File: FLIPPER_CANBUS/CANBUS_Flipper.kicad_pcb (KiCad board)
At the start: 2 copper layers, 67 x 21.3 mm, 33 parts, among them J1 Conn_01x08_Socket, J2 Conn_01x10_Socket, J3 Conn_01x02, J4 Conn_01x02_Socket, U1 MCP2515-xST, U2 MAX3051, Y1 16 Mhz

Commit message: feat(hw): label updated
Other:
- board text removed: "FLIPPER SHIELD CANBUS V1.0"
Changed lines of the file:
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@@
 		(layer "Edge.Cuts")
 	)
-	(gr_text "FLIPPER SHIELD\nCANBUS V1.0"
+	(gr_text "FLIPPER SHIELD\nCANBUS V1.1"
 		(at 139.446 100.584 0)
 		(layer "B.SilkS")

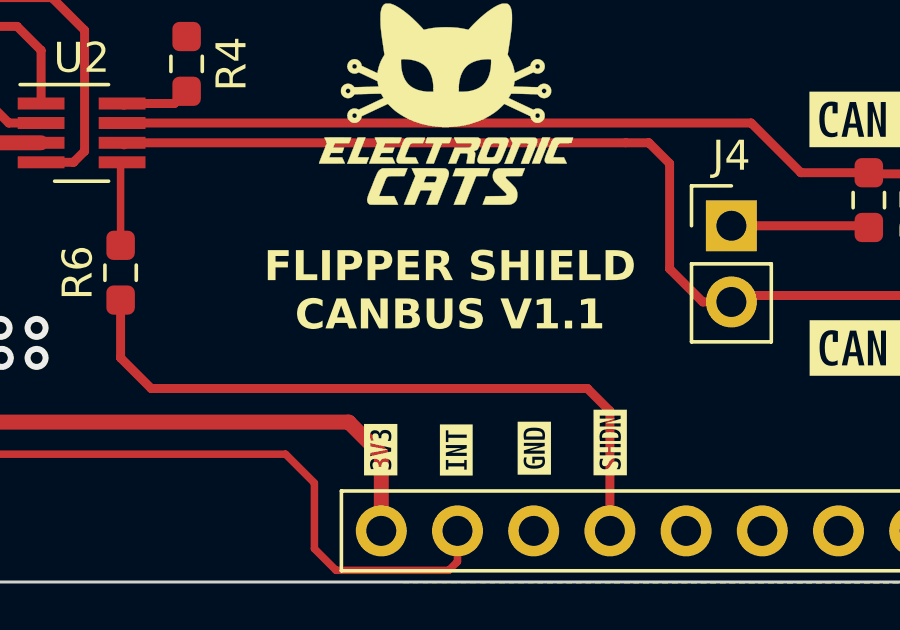
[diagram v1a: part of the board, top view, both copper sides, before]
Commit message: feat: version Label got updated
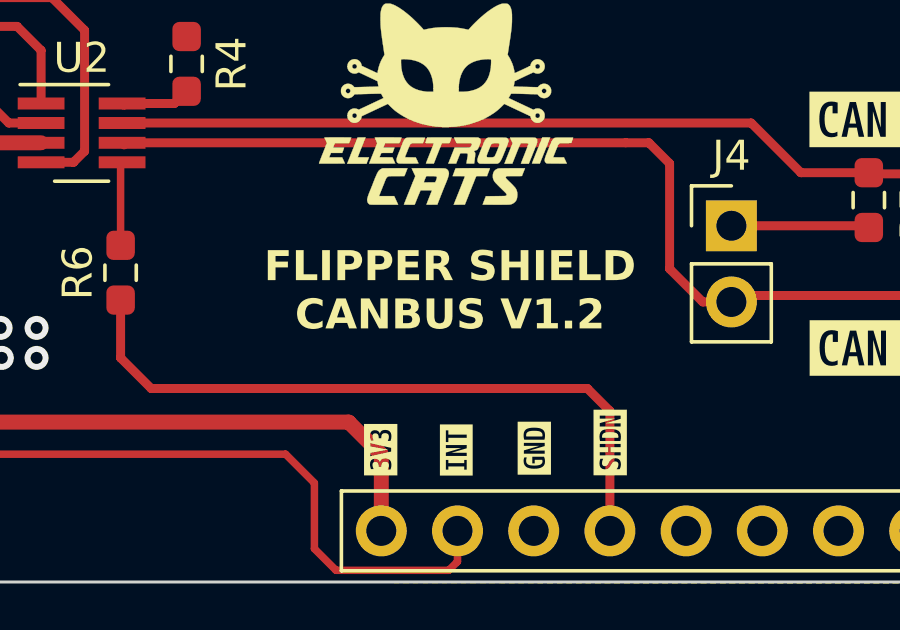
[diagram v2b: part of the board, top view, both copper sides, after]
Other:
- board text added: "FLIPPER SHIELD CANBUS V1.2"
- board text removed: "FLIPPER SHIELD CANBUS V1.1"

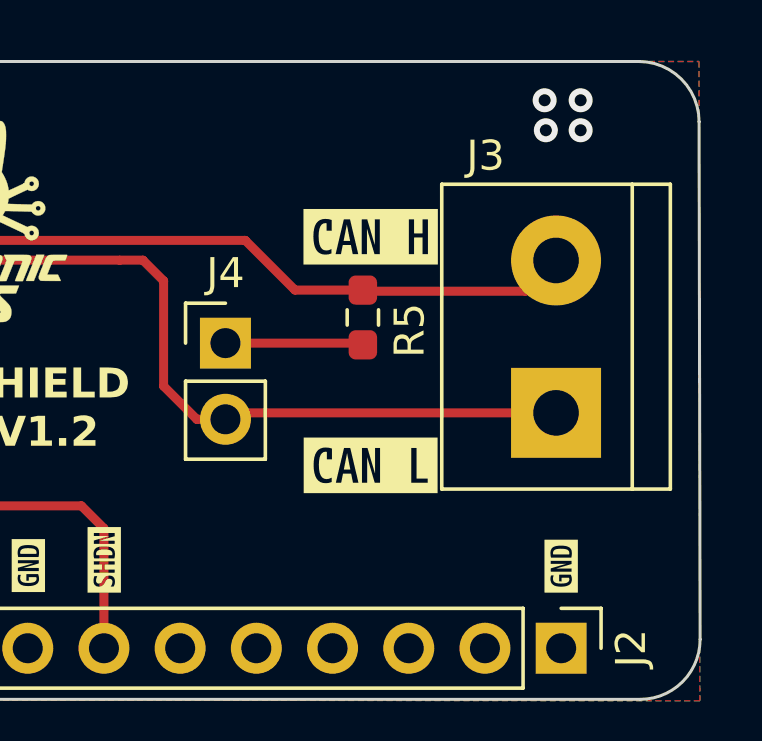
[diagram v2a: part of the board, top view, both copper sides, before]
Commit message: fix: orientation of J3 footprint was wrong
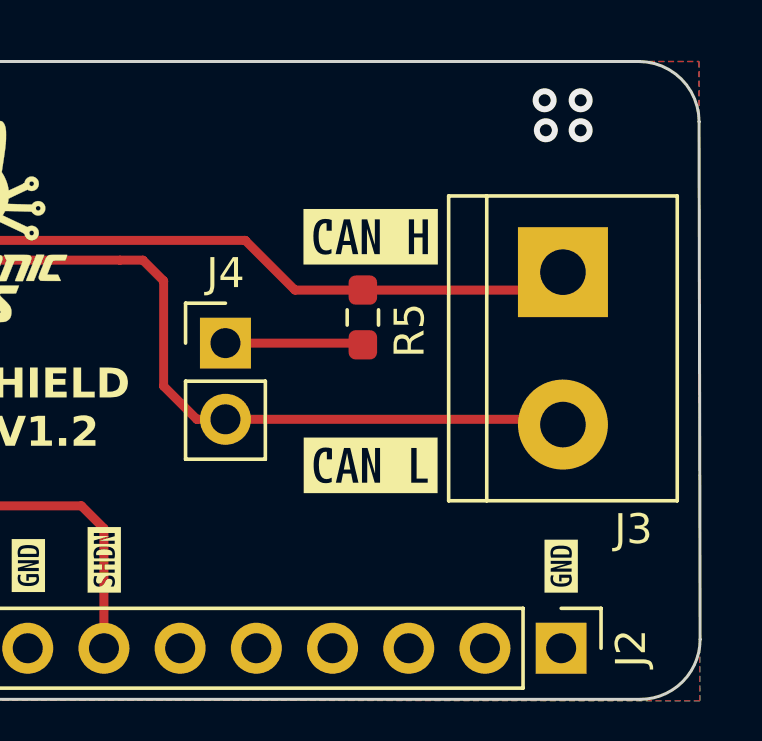
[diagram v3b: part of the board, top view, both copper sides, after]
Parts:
- moved J3 4.70 mm to (171.5, 96.4), turned to -90 degrees
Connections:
- J3 pad 1: /CANL -> /CANH
- J3 pad 2: /CANH -> /CANL
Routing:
- net /CANH: track 33.5 -> 32.5 mm

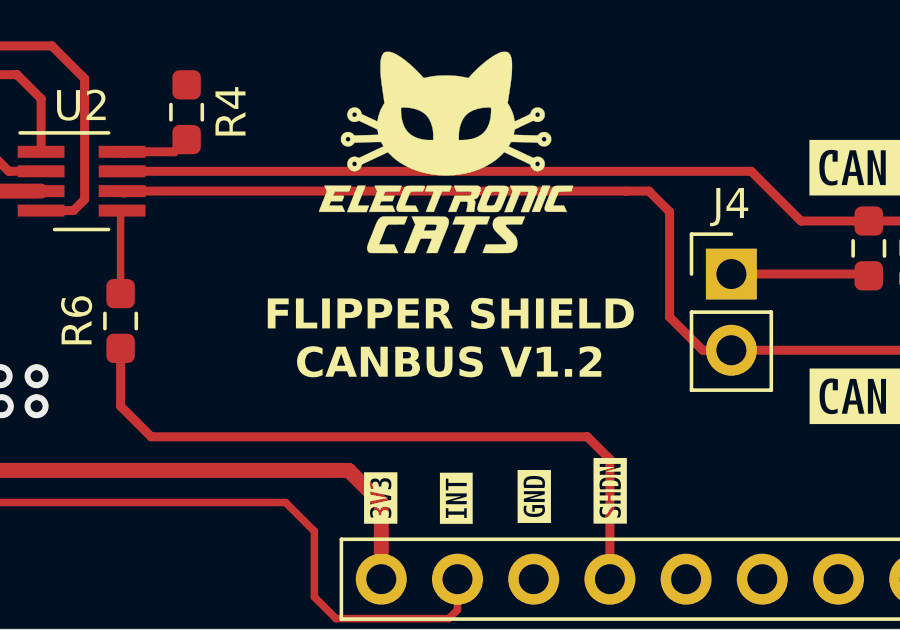
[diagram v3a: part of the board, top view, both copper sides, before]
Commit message: feat: rename addons
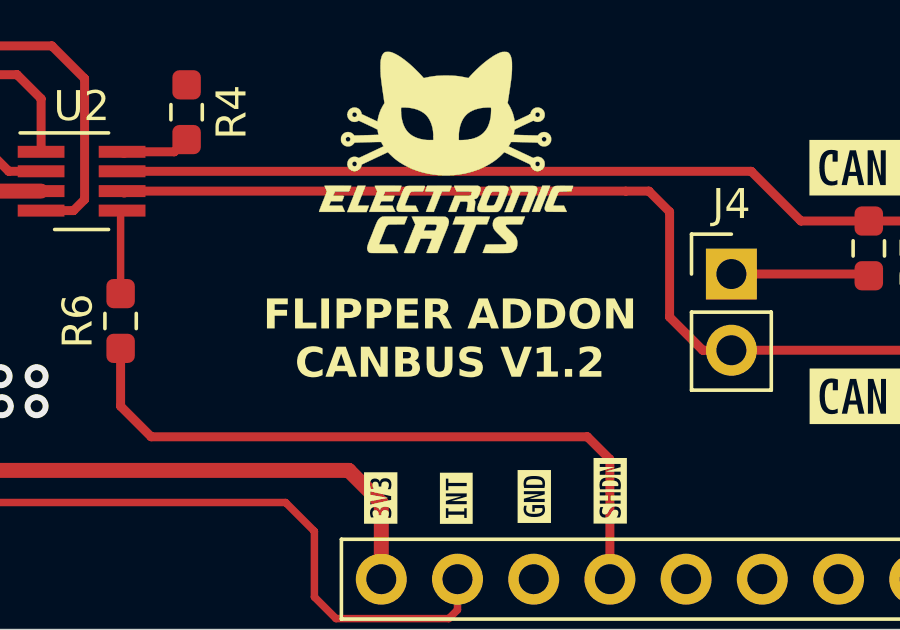
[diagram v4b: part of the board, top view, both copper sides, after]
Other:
- board text added: "FLIPPER ADDON CANBUS V1.2"
- board text removed: "FLIPPER SHIELD CANBUS V1.2"
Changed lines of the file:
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@@
 		(layer "Edge.Cuts")
 	)
-	(gr_text "FLIPPER SHIELD\nCANBUS V1.2"
+	(gr_text "FLIPPER ADDON\nCANBUS V1.2"
 		(at 139.446 100.584 0)
 		(layer "B.SilkS")
@@
 		)
 	)
-	(gr_text "FLIPPER SHIELD\nCANBUS V1.2"
+	(gr_text "FLIPPER ADDON\nCANBUS V1.2"
 		(at 150.88 100.95 0)
 		(layer "F.SilkS")

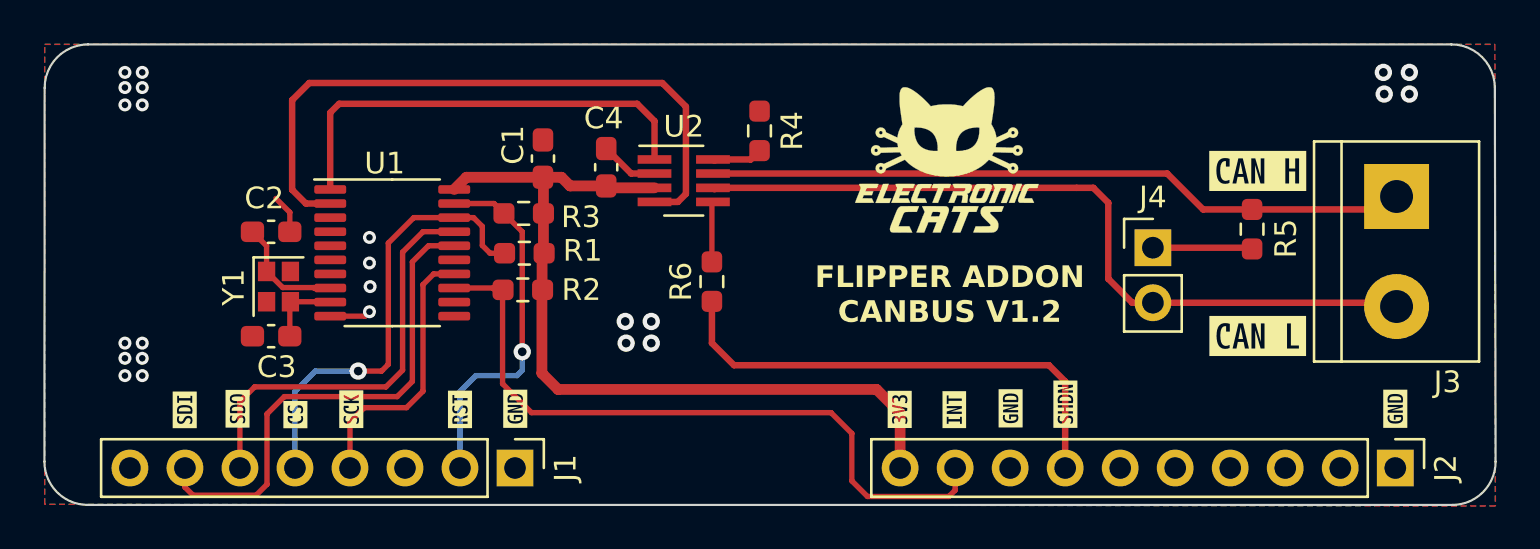
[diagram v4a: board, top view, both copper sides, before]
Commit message: feat(Hw):Update_Schematic_And_Init_Route
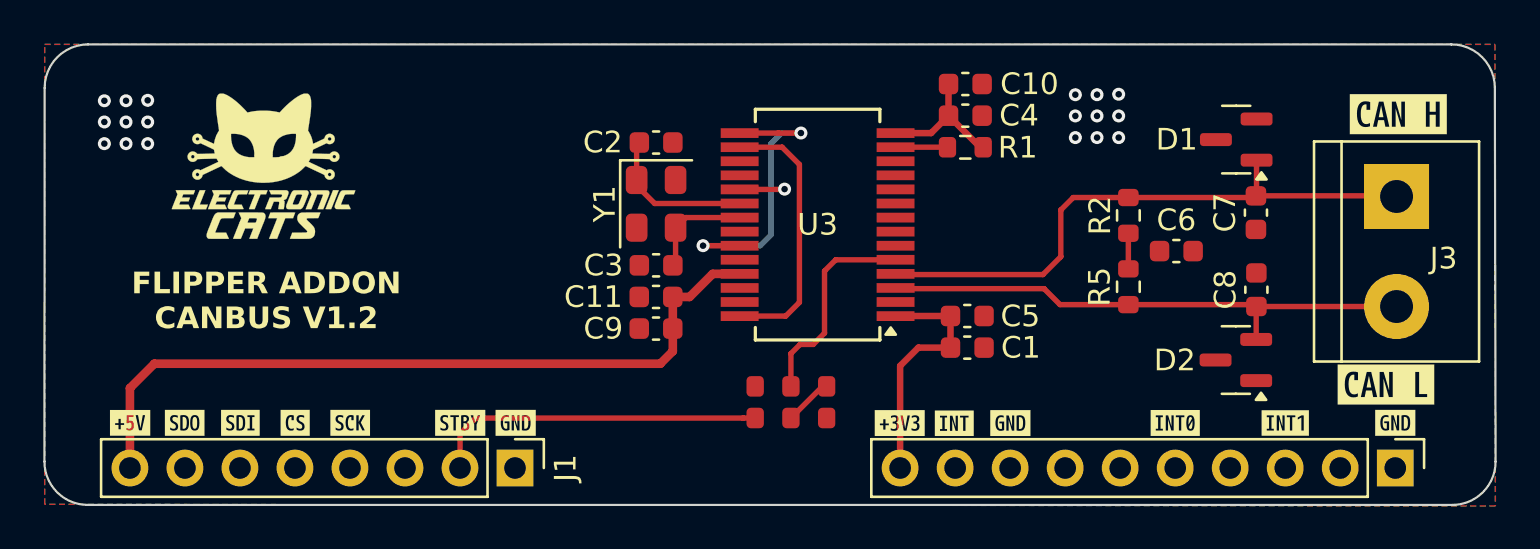
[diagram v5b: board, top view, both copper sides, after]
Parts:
- removed J4: Conn_01x02_Socket, Connector_PinHeader_2.54mm:PinHeader_1x02_P2.54mm_Vertical
- removed R3: 10K, Resistor_SMD:R_0603_1608Metric_Pad0.98x0.95mm_HandSolder
- removed R4, R6: 0, Resistor_SMD:R_0603_1608Metric_Pad0.98x0.95mm_HandSolder
- removed U1: MCP2515-xST, Package_SO:TSSOP-20_4.4x6.5mm_P0.65mm
- removed U2: MAX3051, Package_TO_SOT_SMD:SOT-23-8_Handsoldering
- removed kibuzzard-65B92F42 (x3): G***, kibuzzard-65B92F42
- removed kibuzzard-65B92F61: G***, kibuzzard-65B92F61
- removed kibuzzard-65B92F6C: G***, kibuzzard-65B92F6C
- removed kibuzzard-65B92F78: G***, kibuzzard-65B92F78
- removed kibuzzard-65B92F83: G***, kibuzzard-65B92F83
- removed kibuzzard-65B92F91: G***, kibuzzard-65B92F91
- removed kibuzzard-65B92F9D: G***, kibuzzard-65B92F9D
- removed kibuzzard-65B92FB1: G***, kibuzzard-65B92FB1
- removed kibuzzard-65B92FBC: G***, kibuzzard-65B92FBC
- added C10: 10uF, Capacitor_SMD:C_0603_1608Metric, F.Cu at (151.6, 91.2)
- added C11: 0.1uF, Capacitor_SMD:C_0603_1608Metric, F.Cu at (137.3, 101.1)
- added C5: 0.1uF, Capacitor_SMD:C_0603_1608Metric, F.Cu at (151.7, 101.9)
- added C6: 4.7nF, Capacitor_SMD:C_0603_1608Metric, F.Cu at (161.3, 99.0)
- added C7: 47pF, Capacitor_SMD:C_0603_1608Metric, F.Cu at (165.0, 97.2)
- added C8: 47pF, Capacitor_SMD:C_0603_1608Metric, F.Cu at (165.0, 100.7)
- added C9: 10uF, Capacitor_SMD:C_0603_1608Metric, F.Cu at (137.3, 102.5)
- added D1: MMBZ27VCL-7-F, Package_TO_SOT_SMD:SOT-23, F.Cu at (164.1, 93.8)
- added D2: MMBZ27VCL-7-F, Package_TO_SOT_SMD:SOT-23, F.Cu at (164.1, 104.0)
- added JP1: STBY SEL, Footprints:Jumper, F.Cu at (143.5, 106.7)
- added JP2: STBY, Footprints:Jumper, F.Cu at (143.5, 105.2)
- added U3: MCP251863T-H-SS, Package_SO:SSOP-28_5.3x10.2mm_P0.65mm, F.Cu at (144.8, 97.7)
- added kibuzzard-6930B209: G***, kibuzzard-6930B209, F.Cu at (161.3, 106.9)
- added kibuzzard-6930B295: G***, kibuzzard-6930B295, F.Cu at (153.7, 106.9)
- added kibuzzard-6930B2A6: G***, kibuzzard-6930B2A6, F.Cu at (151.1, 106.9)
- added kibuzzard-6930B2E0: G***, kibuzzard-6930B2E0, F.Cu at (166.4, 106.9)
- added kibuzzard-6930B93D: G***, kibuzzard-6930B93D, F.Cu at (148.6, 106.9)
- added kibuzzard-6930B972: G***, kibuzzard-6930B972, F.Cu at (128.3, 106.9)
- added kibuzzard-6930B9E8: G***, kibuzzard-6930B9E8, F.Cu at (171.4, 106.9)
- added kibuzzard-6930BA32: G***, kibuzzard-6930BA32, F.Cu at (130.8, 106.9)
- added kibuzzard-6930BA54: G***, kibuzzard-6930BA54, F.Cu at (123.2, 106.9)
- added kibuzzard-6930BA73: G***, kibuzzard-6930BA73, F.Cu at (120.7, 106.9)
- added kibuzzard-6930BA9C: G***, kibuzzard-6930BA9C, F.Cu at (115.6, 106.9)
- added kibuzzard-6930BAB6: G***, kibuzzard-6930BAB6, F.Cu at (118.1, 106.9)
- added kibuzzard-6930BAD2: G***, kibuzzard-6930BAD2, F.Cu at (113.0, 106.9)
- C1: value 0.1uF -> 10uF; footprint Capacitor_SMD:C_0603_1608Metric_Pad1.08x0.95mm_HandSolder -> Capacitor_SMD:C_0603_1608Metric
- C2, C3: value 22pF -> 18pF; footprint Capacitor_SMD:C_0603_1608Metric_Pad1.08x0.95mm_HandSolder -> Capacitor_SMD:C_0603_1608Metric
- C4: footprint Capacitor_SMD:C_0603_1608Metric_Pad1.08x0.95mm_HandSolder -> Capacitor_SMD:C_0603_1608Metric
- J3: value Conn_01x02 -> Conn
- R1: footprint Resistor_SMD:R_0603_1608Metric_Pad0.98x0.95mm_HandSolder -> Resistor_SMD:R_0603_1608Metric
- R2: value 10K -> 60; footprint Resistor_SMD:R_0603_1608Metric_Pad0.98x0.95mm_HandSolder -> Resistor_SMD:R_0603_1608Metric
- R5: value 120 -> 60; footprint Resistor_SMD:R_0603_1608Metric_Pad0.98x0.95mm_HandSolder -> Resistor_SMD:R_0603_1608Metric
- Y1: value 16 Mhz -> 40MHz; footprint Crystal:Crystal_SMD_2016-4Pin_2.0x1.6mm -> Crystal:Crystal_SMD_EuroQuartz_MT-4Pin_3.2x2.5mm
- moved G*** 31.6 mm to (119.2, 95.0)
- moved R2 28.2 mm to (159.1, 97.3), turned to -90 degrees
- moved C1 21.4 mm to (151.7, 103.4), turned to 180 degrees
- moved R1 20.9 mm to (151.6, 94.2)
- moved C2 18.2 mm to (137.3, 93.9)
- moved C3 18.1 mm to (137.3, 99.6)
- moved Y1 17.8 mm to (137.3, 96.8)
- moved C4 16.8 mm to (151.6, 92.7), turned to 180 degrees
- moved kibuzzard-65B92FFC 7.00 mm to (171.6, 92.6)
- moved kibuzzard-65B9300E 6.33 mm to (171.0, 105.1)
- moved R5 6.30 mm to (159.1, 100.6)
- moved REF** 4.22 mm to (122.3, 95.9)
- moved G*** 1.65 mm to (149.3, 95.9)
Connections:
- J1 pad 2: /RST -> /STBY
- J2 pad 3: unconnected-(J2-Pin_3-Pad3) -> /INT1
- J2 pad 5: unconnected-(J2-Pin_5-Pad5) -> /INT0
- J2 pad 7: /SHDN -> unconnected-(J2-Pin_7-Pad7)
- R2 pad 1: /INT -> /CANH
- R2 pad 2: +3.3V -> Net-(C6-Pad1)
- R5 pad 1: /CANH -> Net-(C6-Pad1)
- R5 pad 2: Net-(J4-Pin_1) -> /CANL
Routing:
- net +5V: track 0.00 -> 35.5 mm
- net /RXD: track 30.8 -> 0.00 mm
- net /INT: track 32.1 -> 2.08 mm, vias 0 -> 1
- net /SDI: track 23.4 -> 0.00 mm
- net /SHDN: track 23.0 -> 0.00 mm
- net +3.3V: track 38.7 -> 17.8 mm
- net /TXD: track 20.8 -> 0.00 mm
- net /SDO: track 19.4 -> 0.00 mm
- net /CS: track 21.0 -> 2.40 mm, vias 1 -> 0
- net /RST: track 16.9 -> 0.00 mm, vias 1 -> 0
- net /STBY: track 0.00 -> 15.5 mm
- net Net-(U3-TXCAN): track 0.00 -> 13.7 mm, vias 0 -> 2
- net /SCK: track 12.7 -> 0.00 mm
- net Net-(U3-RXCAN): track 0.00 -> 12.5 mm
- net /CANL: track 36.0 -> 25.0 mm
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
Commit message: feat(Hw):Update_Route
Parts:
- moved C6 3.69 mm to (159.5, 102.1), turned to -90 degrees
- moved REF** 3.68 mm to (119.4, 98.0)
- moved G*** 2.12 mm to (149.9, 97.9)
- moved D1 2.02 mm to (162.8, 95.4)
- moved R2 1.82 mm to (160.9, 97.6), turned to 90 degrees
- moved R5 1.81 mm to (160.9, 100.5), turned to 90 degrees
- moved D2 1.79 mm to (162.8, 102.7)
- moved G*** 1.55 mm to (120.7, 95.2)
- moved C1 1.29 mm to (151.7, 102.1)
- moved C3 1.29 mm to (137.3, 98.3)
- moved C11 1.29 mm to (137.3, 99.8)
- moved C2 1.29 mm to (137.3, 92.6)
- moved C5 1.29 mm to (151.7, 100.7)
- moved C9 1.29 mm to (137.3, 101.2)
- moved U3 1.29 mm to (144.8, 96.4)
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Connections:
- net /CANH renamed /CAN+
- net /CANL renamed /CAN-
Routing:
- net /SDO: track 0.00 -> 50.0 mm, vias 0 -> 1
- net /CS: track 2.40 -> 47.6 mm, vias 0 -> 1
- net /SDI: track 0.00 -> 44.6 mm
- net /SCK: track 0.00 -> 36.2 mm
- net /INT0: track 0.00 -> 34.8 mm, vias 0 -> 2
- net /INT1: track 0.00 -> 27.5 mm, vias 0 -> 1
- net /INT: track 2.08 -> 22.7 mm
- net +3.3V: track 17.8 -> 29.7 mm, vias 0 -> 2
- net Net-(C6-Pad1): track 1.64 -> 7.25 mm, vias 0 -> 2
- net GND: track 0.00 -> 3.19 mm, vias 18 -> 38
- net /CAN-: track 25.0 -> 28.1 mm
- net /STB: track 9.82 -> 10.9 mm
- net +5V: track 35.5 -> 36.5 mm
- net /CAN+: track 27.6 -> 28.2 mm
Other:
- board text added: "FLIPPER ADDON CANBUS V2.0"
- board text removed: "FLIPPER ADDON CANBUS V1.2"

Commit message: feat(Hw):Update_Schematic_And_Route
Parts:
- R2, R5: value 60 -> 60.2
- moved C1 2.28 mm to (149.4, 102.1)
- moved C10 2.28 mm to (149.6, 90.8)
- moved C11 2.28 mm to (135.0, 99.8)
- moved C2 2.28 mm to (135.0, 92.6)
- moved C3 2.28 mm to (135.0, 98.3)
- moved C4 2.28 mm to (149.6, 92.3)
- moved C5 2.28 mm to (149.4, 100.6)
- moved C9 2.28 mm to (135.0, 101.2)
- moved G*** 2.28 mm to (147.7, 97.9)
- moved R1 2.28 mm to (149.6, 93.7)
- moved U3 2.28 mm to (142.5, 96.4)
- moved Y1 2.28 mm to (135.0, 95.5)
- moved JP1 1.29 mm to (144.3, 105.6)
- moved JP2 1.29 mm to (144.3, 104.1), turned to 180 degrees
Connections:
- J2 pad 4: unconnected-(J2-Pin_4-Pad4) -> /CLK0
- U3 pad 18: unconnected-(U3-CLKO-Pad18) -> /CLK0
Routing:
- net /CLK0: track 0.00 -> 38.0 mm, vias 0 -> 1
- net /STB: track 10.9 -> 7.44 mm
- net /INT: track 22.7 -> 25.8 mm
- net /INT1: track 27.5 -> 30.0 mm
- net /SDO: track 50.0 -> 47.6 mm
- net /CAN-: track 28.1 -> 30.4 mm
- net /CAN+: track 28.2 -> 30.5 mm
- net /CS: track 47.6 -> 45.3 mm
- net +3.3V: track 29.7 -> 27.9 mm
- net /STBY: track 15.5 -> 17.3 mm
- net /INT0: track 34.8 -> 36.5 mm
- net /SDI: track 44.6 -> 43.1 mm
- net /SCK: track 36.2 -> 34.7 mm
- net Net-(U3-RXCAN): track 12.5 -> 13.3 mm
- net +5V: track 36.5 -> 37.1 mm, vias 0 -> 2
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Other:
- board text added: "INT0"
- board text added: "ON"
- board text added: "STBY"

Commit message: feat(Hw):Update_Schematic_Route_And_Labels
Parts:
- added CLK0: Jumper_2_Open, Jumper:SolderJumper-2_P1.3mm_Open_Pad1.0x1.5mm, F.Cu at (166.1, 105.6)
- moved kibuzzard-6930B2A6 25.4 mm to (125.7, 106.9)
- moved kibuzzard-6930B209 10.2 mm to (151.1, 106.9)
- moved kibuzzard-6930B2E0 5.08 mm to (161.3, 106.9)
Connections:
- J1 pad 3: unconnected-(J1-Pin_3-Pad3) -> /INT
- J2 pad 3: /INT1 -> /CLK
- J2 pad 4: /CLK0 -> unconnected-(J2-Pin_4-Pad4)
- J2 pad 5: /INT0 -> /INT1
- J2 pad 9: /INT -> /INT0
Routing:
- net /INT0: track 36.5 -> 25.1 mm, vias 2 -> 1
- net /INT: track 25.8 -> 31.8 mm
- net /INT1: track 30.0 -> 25.0 mm
- net /CLK: track 0.00 -> 3.55 mm
- net /CLK0: track 38.0 -> 37.2 mm, vias 1 -> 2
- net GND: vias 44 -> 43
